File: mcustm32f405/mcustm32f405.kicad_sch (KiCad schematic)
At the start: 34 parts, among them J2 STM32WORLD_BASE, SW1 TS-1088R-02526, SW2 TS-1088R-02526, U1 AMS1117-3.3, U2 SRV05-4, U3 STM32F405RGTx, Y1 X_16MHZ

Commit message: Hmmmm
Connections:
- net +3.3V is gone; now on net +3V3: R3.1
- no-connect marks 2 -> 21
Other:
- moved on the sheet: C2, JP1

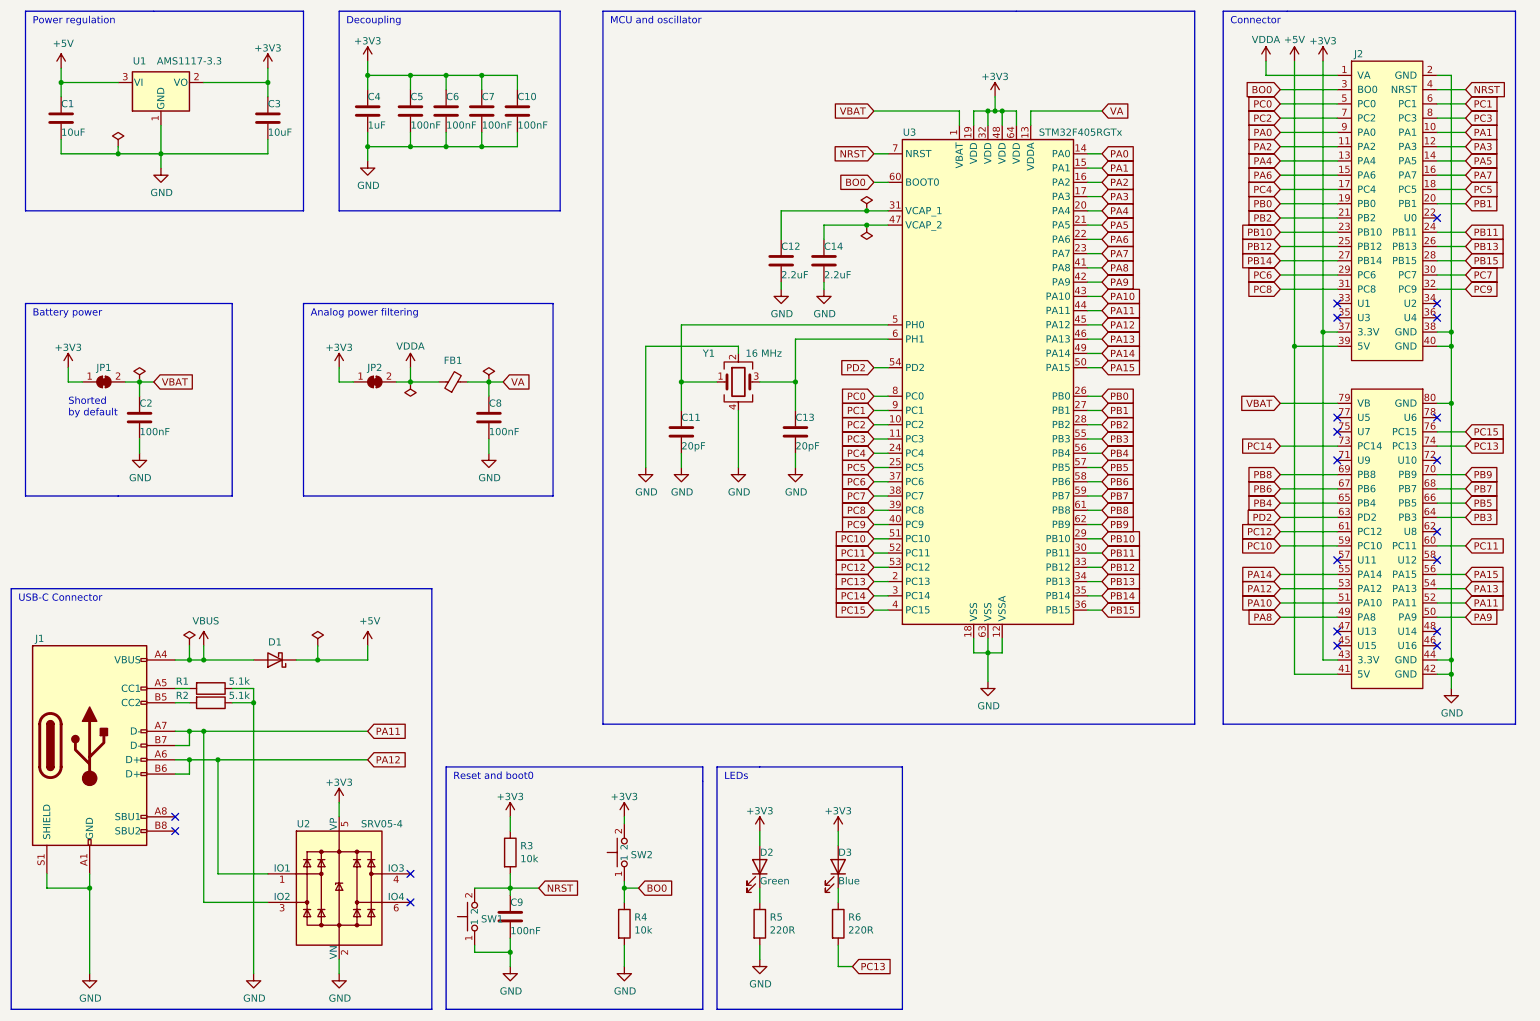
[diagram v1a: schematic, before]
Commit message: MCUSTM32F405 should be ready for order
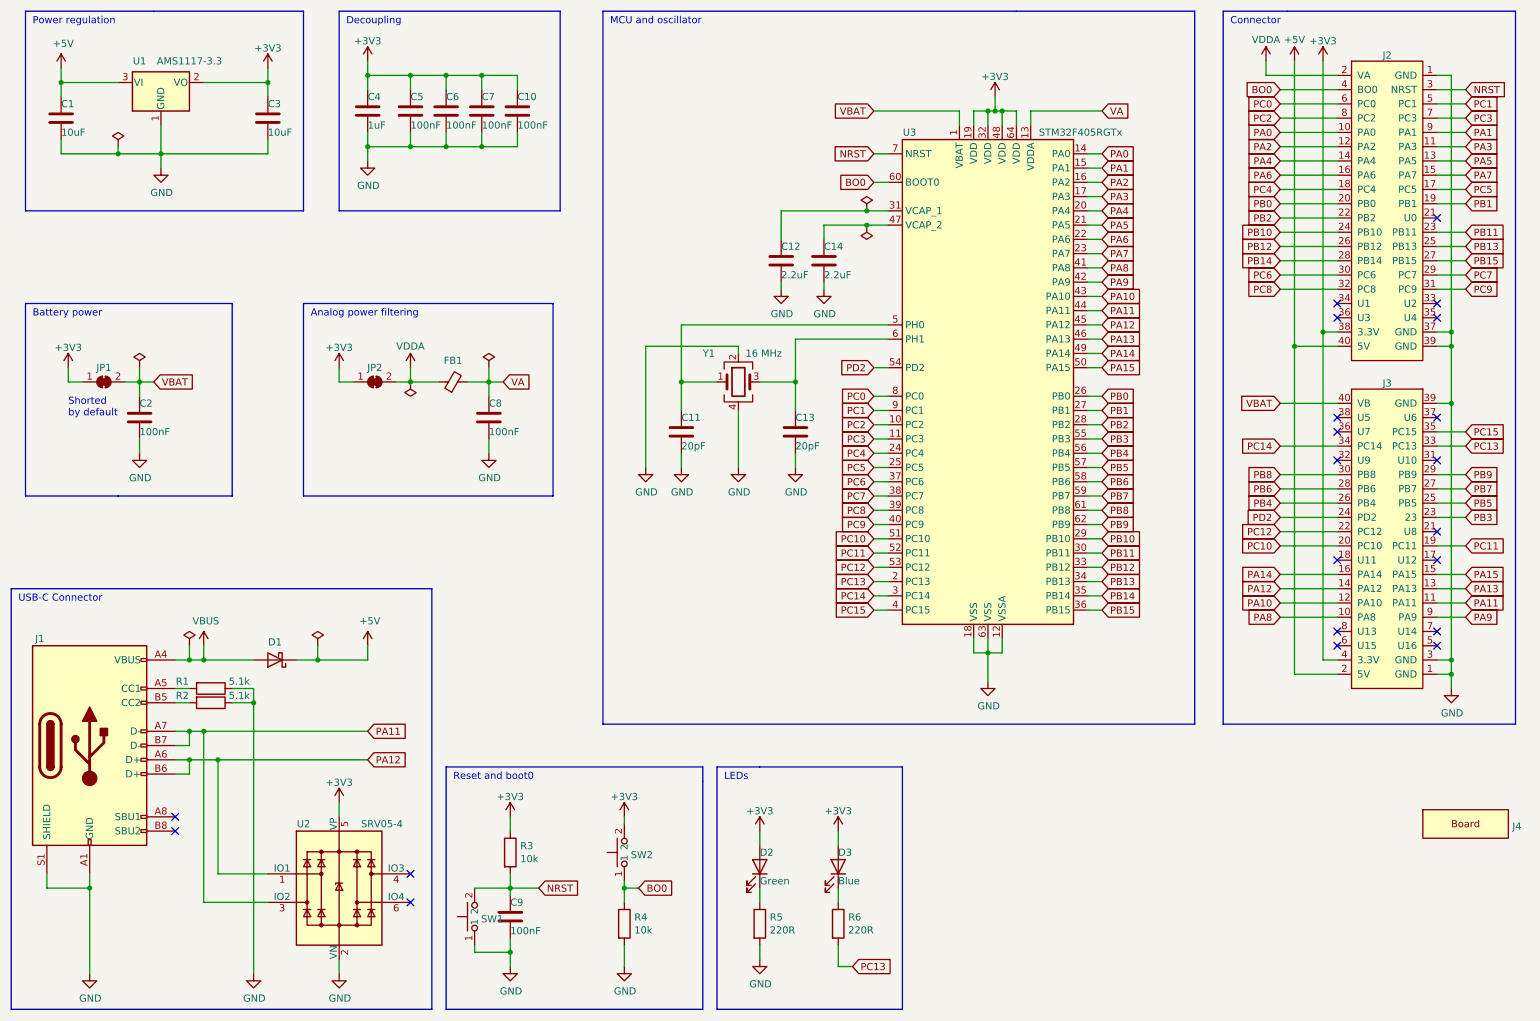
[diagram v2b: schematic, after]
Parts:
- removed J2: STM32WORLD_BASE, stm32world:STM32WORLD_BASE, symbol stm32world:STM32WORLD_BASE
- added J2: STM32WORLD_CONNECTOR_1, stm32world:PinSocket_2x20_P2.54mm_Vertical_Stackable, symbol stm32world:STM32WORLD_CONNECTOR_1
- added J3: STM32WORLD_CONNECTOR_2, stm32world:PinSocket_2x20_P2.54mm_Vertical_Stackable, symbol stm32world:STM32WORLD_CONNECTOR_2
- added J4: STM32WORLD_BOARD, stm32world:STM32WORLD_BOARD, symbol stm32world:STM32WORLD_BOARD
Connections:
- net +3V3: now also J2.38 (3.3V), J3.4 (3.3V)
- net +5V: now also J2.40 (5V), J3.2 (5V)
- net BO0: now also J2.4 (BO0)
- net GND: now also J2.1 (GND), J2.37 (GND), J2.39 (GND), J3.1 (GND), J3.3 (GND), J3.39 (GND)
- net NRST: now also J2.3 (NRST)
- net PA0: now also J2.10 (PA0)
- net PA1: now also J2.9 (PA1)
- net PA10: now also J3.12 (PA10)
- net PA11: now also J3.11 (PA11)
- net PA12: now also J3.14 (PA12)
- net PA13: now also J3.13 (PA13)
- net PA14: now also J3.16 (PA14)
- net PA15: now also J3.15 (PA15)
- net PA2: now also J2.12 (PA2)
- net PA3: now also J2.11 (PA3)
- net PA4: now also J2.14 (PA4)
- net PA5: now also J2.13 (PA5)
- net PA6: now also J2.16 (PA6)
- net PA7: now also J2.15 (PA7)
- net PA8: now also J3.10 (PA8)
- net PA9: now also J3.9 (PA9)
- net PB0: now also J2.20 (PB0)
- net PB1: now also J2.19 (PB1)
- net PB10: now also J2.24 (PB10)
- net PB11: now also J2.23 (PB11)
- net PB12: now also J2.26 (PB12)
- net PB13: now also J2.25 (PB13)
- net PB14: now also J2.28 (PB14)
- net PB15: now also J2.27 (PB15)
- net PB2: now also J2.22 (PB2)
- net PB3: now also J3.23
- net PB4: now also J3.26 (PB4)
- net PB5: now also J3.25 (PB5)
- net PB6: now also J3.28 (PB6)
- net PB7: now also J3.27 (PB7)
- net PB8: now also J3.30 (PB8)
- net PB9: now also J3.29 (PB9)
- net PC0: now also J2.6 (PC0)
- net PC1: now also J2.5 (PC1)
- net PC10: now also J3.20 (PC10)
- net PC11: now also J3.19 (PC11)
- net PC12: now also J3.22 (PC12)
- net PC13: now also J3.33 (PC13)
- net PC14: now also J3.34 (PC14)
- net PC15: now also J3.35 (PC15)
- net PC2: now also J2.8 (PC2)
- net PC3: now also J2.7 (PC3)
- net PC4: now also J2.18 (PC4)
- net PC5: now also J2.17 (PC5)
- net PC6: now also J2.30 (PC6)
- net PC7: now also J2.29 (PC7)
- net PC8: now also J2.32 (PC8)
- net PC9: now also J2.31 (PC9)
- net PD2: now also J3.24 (PD2)
- net VBAT: now also J3.40 (VB)
- net VDDA: now also J2.2 (VA)

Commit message: Ready to order mcustm32f405
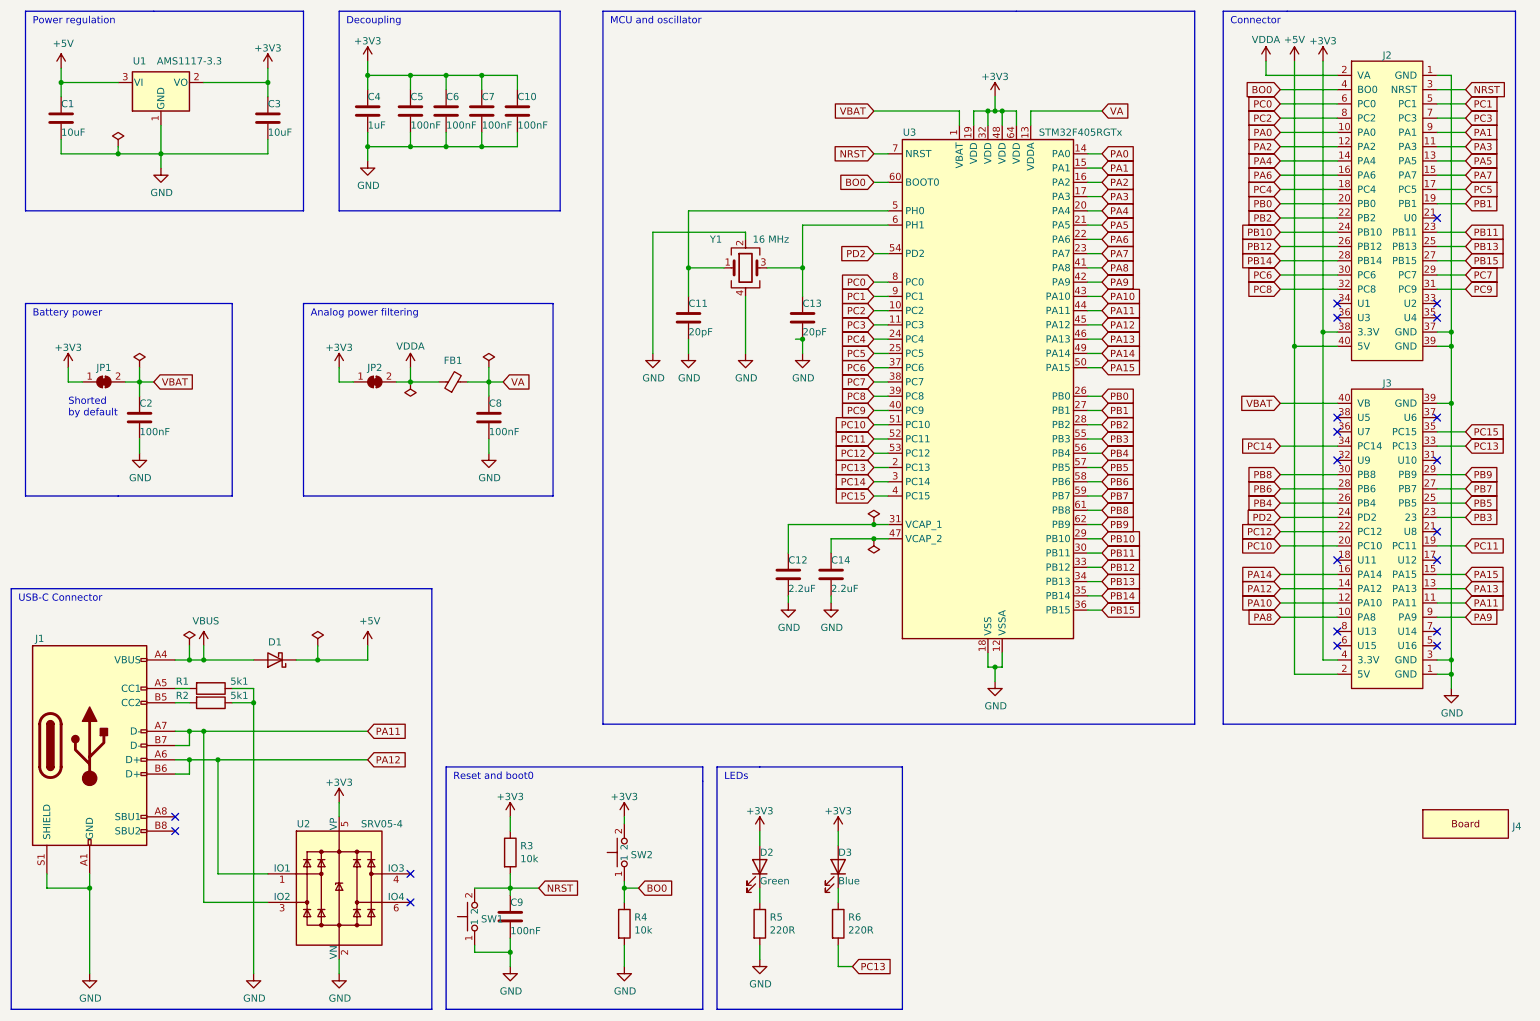
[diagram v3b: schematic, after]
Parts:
- R1, R2: Display 5.1k -> 5k1
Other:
- moved on the sheet: C11, C12, C13, C14, Y1

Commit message: Hmmm
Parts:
- removed U2: SRV05-4, Package_TO_SOT_SMD:SOT-23-6, symbol stm32world:SRV05-4
- added D4: PSM712, Package_TO_SOT_SMD:SOT-23, symbol Power_Protection:SP0502BAHT
- added JP3, JP4: SolderJumper_2_Bridged, Jumper:SolderJumper-2_P1.3mm_Bridged_RoundedPad1.0x1.5mm, symbol stm32world:SolderJumper_2_Bridged
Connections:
- net BO0: now also JP4.1 (A); no longer J2.4 (BO0)
- net GND: now also D4.3 (A)
- net NRST: now also JP3.1 (A); no longer J2.3 (NRST)
- net PA11: now also D4.1 (K)
- net PA12: now also D4.2 (K)
- new net HBO0: J2.4 (BO0), JP4.2 (B)
- new net HNRST: J2.3 (NRST), JP3.2 (B)
- no-connect marks 21 -> 19
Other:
- moved on the sheet: C11, C12, C13, C14, C9, D1, D2, D3, J2, J3, R3, R4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

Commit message: Jumpers for nrst and b0 on header.
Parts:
- removed JP3, JP4: SolderJumper_2_Bridged, Jumper:SolderJumper-2_P1.3mm_Bridged_RoundedPad1.0x1.5mm, symbol stm32world:SolderJumper_2_Bridged
- added JP3, JP4: ~, Jumper:SolderJumper-2_P1.3mm_Open_RoundedPad1.0x1.5mm, symbol Jumper:SolderJumper_2_Open
- renumbered C9 to C6, C6 to C7, C7 to C8, C8 to C9, D4 to D1, D1 to D2, D2 to D3, D3 to D4, U3 to U2
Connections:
- net BO0: now also JP4.1 (A)
- net HBO0: now also JP4.2 (B)
- net HNRST: now also JP3.2 (B)
- net NRST: now also JP3.1 (A)

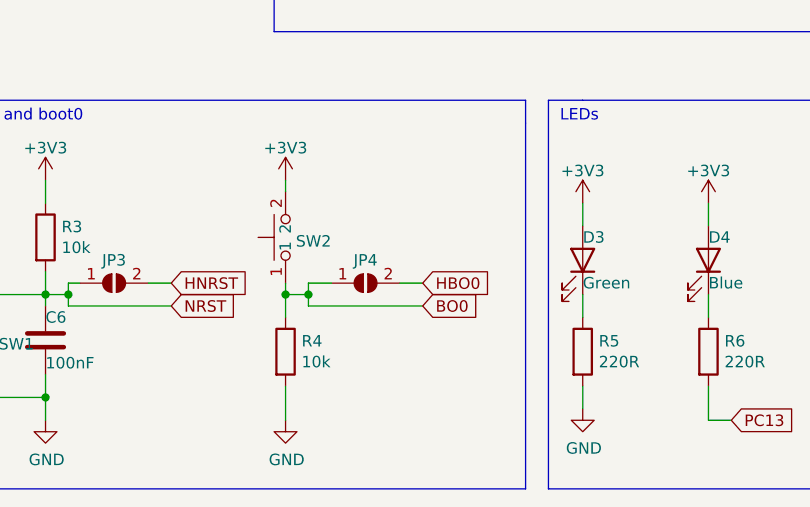
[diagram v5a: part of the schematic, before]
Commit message: Wired B0 to PC15 so it can be read
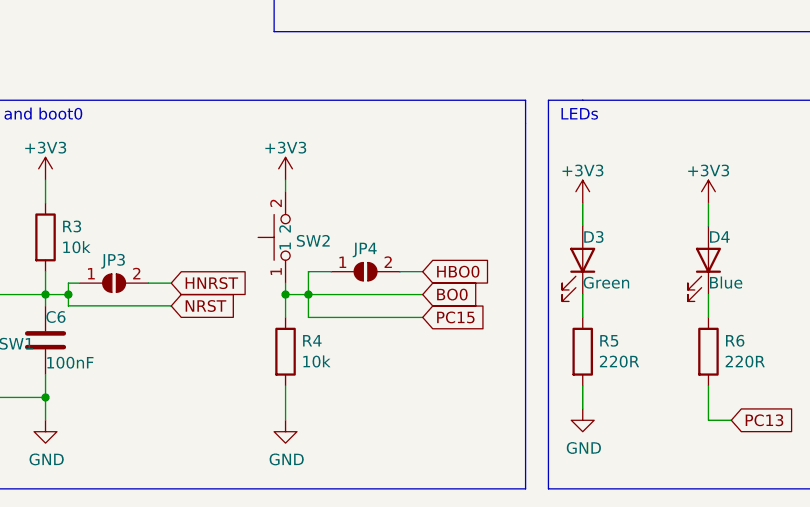
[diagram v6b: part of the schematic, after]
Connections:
- net PC15 is gone; now on net BO0: J3.35 (PC15), U2.4 (PC15)
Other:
- moved on the sheet: JP4
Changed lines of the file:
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@@
     (stroke (width 0) (type default))
   )
+  (wire (pts (xy 132.08 173.99) (xy 119.38 173.99))
+    (stroke (width 0) (type default))
+  )
   (wire (pts (xy 45.72 128.27) (xy 45.72 130.81))
     (stroke (width 0) (type default))
@@
     (stroke (width 0) (type default))
   )
-  (wire (pts (xy 119.38 171.45) (xy 119.38 170.18))
+  (wire (pts (xy 119.38 171.45) (xy 119.38 168.91))
     (stroke (width 0) (type default))
   )
@@
     (stroke (width 0) (type default))
   )
-  (wire (pts (xy 119.38 172.72) (xy 119.38 171.45))
-    (stroke (width 0) (type default))
-  )
   (wire (pts (xy 191.77 33.02) (xy 204.47 33.02))
     (stroke (width 0) (type default))
@@
     (stroke (width 0) (type default))
   )
-  (wire (pts (xy 119.38 170.18) (xy 121.92 170.18))
+  (wire (pts (xy 119.38 168.91) (xy 121.92 168.91))
     (stroke (width 0) (type default))
   )
@@
     (stroke (width 0) (type default))
   )
-  (wire (pts (xy 132.08 172.72) (xy 119.38 172.72))
+  (wire (pts (xy 132.08 171.45) (xy 119.38 171.45))
     (stroke (width 0) (type default))
   )
@@
     (stroke (width 0) (type default))
   )
+  (wire (pts (xy 119.38 173.99) (xy 119.38 171.45))
+    (stroke (width 0) (type default))
+  )
   (wire (pts (xy 201.93 101.6) (xy 204.47 101.6))
     (stroke (width 0) (type default))
@@
     (stroke (width 0) (type default))
   )
-  (wire (pts (xy 129.54 170.18) (xy 132.08 170.18))
+  (wire (pts (xy 129.54 168.91) (xy 132.08 168.91))
     (stroke (width 0) (type default))
   )
@@
     )
   )
-  (global_label "HBO0" (shape input) (at 132.08 170.18 0) (fields_autoplaced)
+  (global_label "HBO0" (shape input) (at 132.08 168.91 0) (fields_autoplaced)
     (effects (font (size 1.27 1.27)) (justify left))
-    (property "Intersheetrefs" "${INTERSHEET_REFS}" (at 139.5515 170.18 0)
+    (property "Intersheetrefs" "${INTERSHEET_REFS}" (at 139.5515 168.91 0)
       (effects (font (size 1.27 1.27)) (justify left) hide)
     )
@@
     )
   )
+  (global_label "PC15" (shape input) (at 132.08 173.99 0) (fields_autoplaced)
+    (effects (font (size 1.27 1.27)) (justify left))
+    (property "Intersheetrefs" "${INTERSHEET_REFS}" (at 139.37 173.99 0)
+      (effects (font (size 1.27 1.27)) (justify left) hide)
+    )
+  )
   (global_label "PA0" (shape input) (at 237.49 36.83 180) (fields_autoplaced)
     (effects (font (size 1.27 1.27)) (justify right))
@@
     )
   )
-  (global_label "BO0" (shape input) (at 132.08 172.72 0) (fields_autoplaced)
+  (global_label "BO0" (shape input) (at 132.08 171.45 0) (fields_autoplaced)
     (effects (font (size 1.27 1.27)) (justify left))
-    (property "Intersheetrefs" "${INTERSHEET_REFS}" (at 78.74 85.09 0)
+    (property "Intersheetrefs" "${INTERSHEET_REFS}" (at 78.74 83.82 0)
       (effects (font (size 1.27 1.27)) hide)
     )
@@
     )
   )
-  (symbol (lib_id "Jumper:SolderJumper_2_Open") (at 125.73 170.18 0) (unit 1)
+  (symbol (lib_id "Jumper:SolderJumper_2_Open") (at 125.73 168.91 0) (unit 1)
     (in_bom yes) (on_board yes) (dnp no)
-    (property "Reference" "JP4" (at 125.73 167.64 0)
+    (property "Reference" "JP4" (at 125.73 166.37 0)
       (effects (font (size 1.27 1.27)))
     )
-    (property "Value" "~" (at 125.73 166.37 0)
+    (property "Value" "~" (at 125.73 165.1 0)
       (effects (font (size 1.27 1.27)) hide)
     )
-    (property "Footprint" "Jumper:SolderJumper-2_P1.3mm_Open_RoundedPad1.0x1.5mm" (at 125.73 170.18 0)
+    (property "Footprint" "Jumper:SolderJumper-2_P1.3mm_Open_RoundedPad1.0x1.5mm" (at 125.73 168.91 0)
       (effects (font (size 1.27 1.27)) hide)
     )
-    (property "Datasheet" "~" (at 125.73 170.18 0)
+    (property "Datasheet" "~" (at 125.73 168.91 0)
       (effects (font (size 1.27 1.27)) hide)
     )
